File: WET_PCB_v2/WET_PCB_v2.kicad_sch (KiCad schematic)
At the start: 38 parts, among them J1 Barrel jack, J10 POGO1, J11 Conn_01x09_Pin, J12 Conn_01x09_Pin, J2 Power input, J3 Jumper, J35 Programming, J36 LED_POWER, J4 Coil plug, J5 Vsense_ADC1_IN1, J6 Pluggable Terminal Block, J7 Conn_01x09_Pin, J8 Conn_01x09_Pin, J9 POGO2, U1 Opamp_Quad

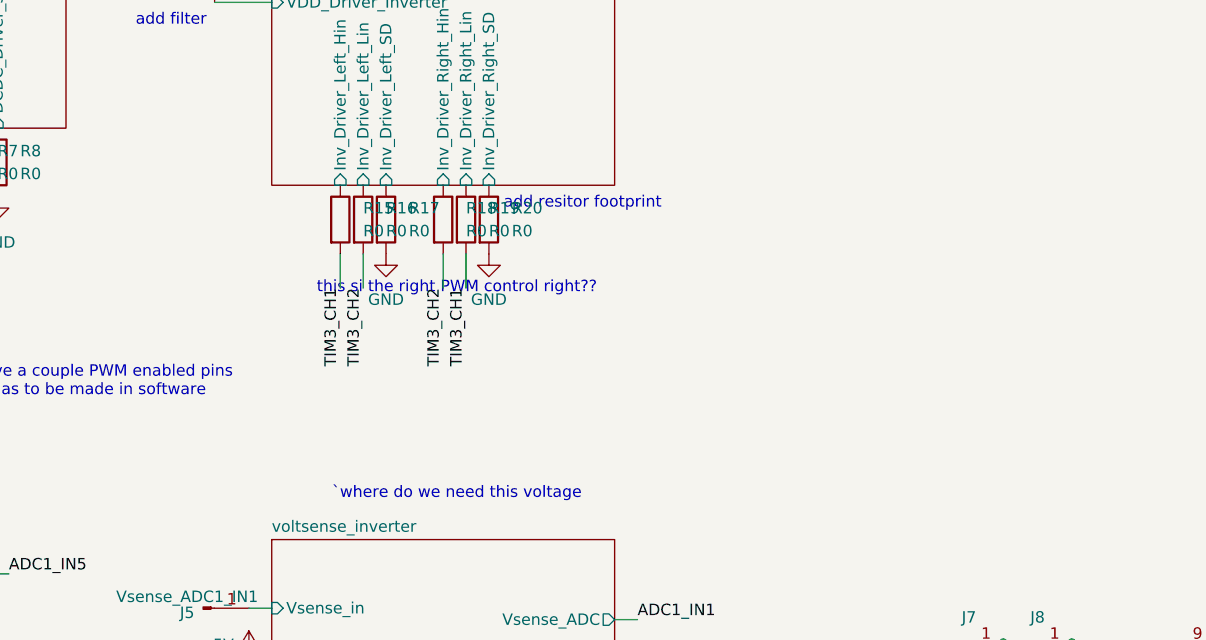
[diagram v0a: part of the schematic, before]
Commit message: most routing done. to do: 12v routing, test points, deco, checking clearance
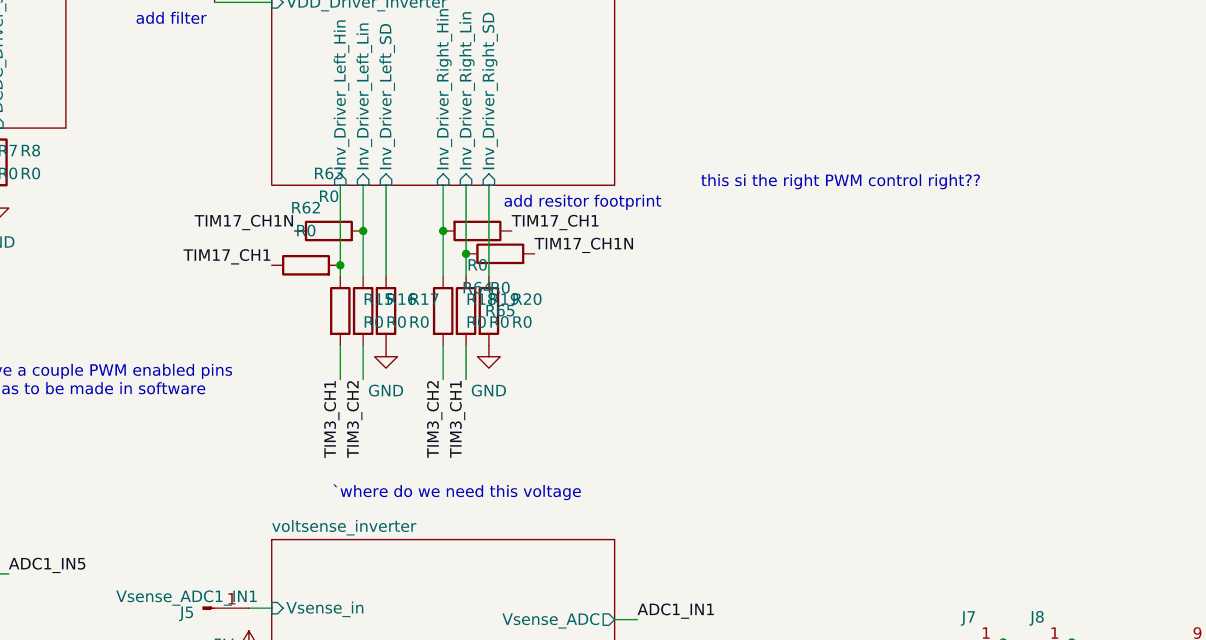
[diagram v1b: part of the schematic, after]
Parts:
- added R62, R63, R64, R65: R0, Resistor_SMD:R_0805_2012Metric_Pad1.20x1.40mm_HandSolder, symbol Device:R
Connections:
- net TIM17_CH1: now also R62.1, R64.1
- net TIM17_CH1N: now also R63.1, R65.2
- net inverter/Inv_Driver_Left_Hin: now also R62.2
- net inverter/Inv_Driver_Left_Lin: now also R63.2
- net inverter/Inv_Driver_Right_Hin: now also R64.2
- net inverter/Inv_Driver_Right_Lin: now also R65.1
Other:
- moved on the sheet: R15, R16, R17, R18, R19, R20

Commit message: fixed some mistakes added debug header
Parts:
- added J37: PRGM_DBG, Connector_PinSocket_2.54mm:PinSocket_1x02_P2.54mm_Vertical, symbol Connector:Conn_01x02_Pin
- J35: value Programming -> PRGM_DBG
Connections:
- net at J35.1 (Pin_1), J9.1 (Pin_1), U2.20 (POGO_PRG): now also J37.1 (Pin_1)
- net at J10.1 (Pin_1), J35.2 (Pin_2), U2.19 (POGO_PRG): now also J37.2 (Pin_2)
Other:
- note removed: "look for other UV LEDs"
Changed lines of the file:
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@@
 		)
 	)
-	(text "look for other UV LEDs"
-		(exclude_from_sim no)
-		(at 52.324 115.57 0)
-		(effects
-			(font
-				(size 1.27 1.27)
-			)
-		)
-	)
 	(text "`where do we need this voltage"
 		(exclude_from_sim no)
@@
 	)
 	(junction
+		(at 381 166.37)
+		(diameter 0)
+		(color 0 0 0 0)
+	)
+	(junction
 		(at 294.64 142.24)
 		(diameter 0)
@@
 	)
 	(junction
+		(at 378.46 170.18)
+		(diameter 0)
+		(color 0 0 0 0)
+	)
+	(junction
 		(at 370.84 162.56)
 		(diameter 0)
@@
 	(wire
 		(pts
+			(xy 378.46 170.18) (xy 384.81 170.18)
+		)
+		(stroke
+			(width 0)
+			(type default)
+		)
+	)
+	(wire
+		(pts
 			(xy 287.02 149.86) (xy 294.64 149.86)
 		)
@@
 	(wire
 		(pts
+			(xy 381 166.37) (xy 373.38 166.37)
+		)
+		(stroke
+			(width 0)
+			(type default)
+		)
+	)
+	(wire
+		(pts
 			(xy 132.08 146.05) (xy 134.62 146.05)
 		)
@@
 	(wire
 		(pts
+			(xy 378.46 170.18) (xy 378.46 172.72)
+		)
+		(stroke
+			(width 0)
+			(type default)
+		)
+	)
+	(wire
+		(pts
 			(xy 287.02 152.4) (xy 294.64 152.4)
 		)
@@
 	(wire
 		(pts
+			(xy 381 166.37) (xy 381 172.72)
+		)
+		(stroke
+			(width 0)
+			(type default)
+		)
+	)
+	(wire
+		(pts
 			(xy 29.21 38.1) (xy 39.37 38.1)
 		)
@@
 	(wire
 		(pts
-			(xy 382.27 166.37) (xy 373.38 166.37)
+			(xy 382.27 166.37) (xy 381 166.37)
 		)
 		(stroke
@@
 	(wire
 		(pts
-			(xy 367.03 170.18) (xy 384.81 170.18)
+			(xy 367.03 170.18) (xy 378.46 170.18)
 		)
 		(stroke
@@
 			)
 		)
-		(property "Value" "Programming"
-			(at 387.604 159.766 0)
+		(property "Value" "PRGM_DBG"
+			(at 391.922 164.846 90)
 			(show_name no)
 			(do_not_autoplace no)
@@
 					(unit 1)
 				)
+			)
+		)
+	)
+	(symbol
+		(lib_id "Connector:Conn_01x02_Pin")
+		(at 378.46 177.8 90)
+		(unit 1)
+		(body_style 1)
+		(exclude_from_sim no)
+		(in_bom yes)
+		(on_board yes)
+		(in_pos_files yes)
+		(dnp no)
+		(property "Reference" "J37"
+			(at 381.762 176.276 0)
+			(show_name no)
+			(do_not_autoplace no)
+			(effects
+				(font
+					(size 1.27 1.27)
+				)
+			)
+		)
+		(property "Value" "PRGM_DBG"
+			(at 379.222 180.086 90)
+			(show_name no)
+			(do_not_autoplace no)
+			(effects
+				(font
+					(size 1.27 1.27)
+				)
+			)
+		)
+		(property "Footprint" "Connector_PinSocket_2.54mm:PinSocket_1x02_P2.54mm_Vertical"
+			(at 378.46 177.8 0)
+			(hide yes)
+			(show_name no)
+			(do_not_autoplace no)
+			(effects
+				(font
+					(size 1.27 1.27)
+				)
+			)
+		)
+		(property "Datasheet" ""
+			(at 378.46 177.8 0)
+			(hide yes)
+			(show_name no)
+			(do_not_autoplace no)
+			(effects
+				(font
+					(size 1.27 1.27)
+				)
+			)
+		)
+		(property "Description" "Generic connector, single row, 01x02, script generated"
+			(at 378.46 177.8 0)
+			(hide yes)
+			(show_name no)
+			(do_not_autoplace no)
+			(effects
+				(font
+					(size 1.27 1.27)
+				)
+			)
+		)
+		(pin "1"
+		)
+		(pin "2"
+		)
+		(instances
+			(project "WET_PCB_v2"
+				(path "/13451c35-1666-47d9-9525-8d8125ba1cf3"
+					(reference "J37")
+					(unit 1)
+				)

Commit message: labels
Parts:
- renumbered R3 to JMP1, R15 to JMP10, R16 to JMP11, R17 to JMP12, R18 to JMP13, R19 to JMP14, R64 to JMP15, R20 to JMP16, R65 to JMP17, R5 to JMP2, R6 to JMP3, R7 to JMP4, R8 to JMP5, R12 to JMP6, R14 to JMP7, R62 to JMP8, R63 to JMP9
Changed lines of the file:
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@@
 		(dnp no)
 		(fields_autoplaced yes)
-		(property "Reference" "R15"
+		(property "Reference" "JMP10"
 			(at 215.9 99.0599 0)
 			(show_name no)
@@
 			(project "WET_PCB_v2"
 				(path "/13451c35-1666-47d9-9525-8d8125ba1cf3"
-					(reference "R15")
+					(reference "JMP10")
 					(unit 1)
 				)
@@
 		(dnp no)
 		(fields_autoplaced yes)
-		(property "Reference" "R20"
+		(property "Reference" "JMP16"
 			(at 232.41 99.0599 0)
 			(show_name no)
@@
 			(project "WET_PCB_v2"
 				(path "/13451c35-1666-47d9-9525-8d8125ba1cf3"
-					(reference "R20")
+					(reference "JMP16")
 					(unit 1)
 				)
@@
 		(dnp no)
 		(fields_autoplaced yes)
-		(property "Reference" "R19"
+		(property "Reference" "JMP14"
 			(at 229.87 99.0599 0)
 			(show_name no)
@@
 			(project "WET_PCB_v2"
 				(path "/13451c35-1666-47d9-9525-8d8125ba1cf3"
-					(reference "R19")
+					(reference "JMP14")
 					(unit 1)
 				)
@@
 		(dnp no)
 		(fields_autoplaced yes)
-		(property "Reference" "R18"
+		(property "Reference" "JMP13"
 			(at 227.33 99.0599 0)
 			(show_name no)
@@
 			(project "WET_PCB_v2"
 				(path "/13451c35-1666-47d9-9525-8d8125ba1cf3"
-					(reference "R18")
+					(reference "JMP13")
 					(unit 1)
 				)
@@
 		(dnp no)
 		(fields_autoplaced yes)
-		(property "Reference" "R3"
+		(property "Reference" "JMP1"
 			(at 152.4 87.6299 0)
 			(show_name no)
@@
 			(project "WET_PCB_v2"
 				(path "/13451c35-1666-47d9-9525-8d8125ba1cf3"
-					(reference "R3")
+					(reference "JMP1")
 					(unit 1)
 				)
@@
 		(dnp no)
 		(fields_autoplaced yes)
-		(property "Reference" "R64"
+		(property "Reference" "JMP15"
 			(at 228.6 97.79 90)
 			(show_name no)
@@
 			(project "WET_PCB_v2"
 				(path "/13451c35-1666-47d9-9525-8d8125ba1cf3"
-					(reference "R64")
+					(reference "JMP15")
 					(unit 1)
 				)
@@
 		(dnp no)
 		(fields_autoplaced yes)
-		(property "Reference" "R62"
+		(property "Reference" "JMP8"
 			(at 209.55 88.9 90)
 			(show_name no)
@@
 			(project "WET_PCB_v2"
 				(path "/13451c35-1666-47d9-9525-8d8125ba1cf3"
-					(reference "R62")
+					(reference "JMP8")
 					(unit 1)
 				)
@@
 		(dnp no)
 		(fields_autoplaced yes)
-		(property "Reference" "R17"
+		(property "Reference" "JMP12"
 			(at 220.98 99.0599 0)
 			(show_name no)
@@
 			(project "WET_PCB_v2"
 				(path "/13451c35-1666-47d9-9525-8d8125ba1cf3"
-					(reference "R17")
+					(reference "JMP12")
 					(unit 1)
 				)
@@
 		(dnp no)
 		(fields_autoplaced yes)
-		(property "Reference" "R5"
+		(property "Reference" "JMP2"
 			(at 160.02 87.6299 0)
 			(show_name no)
@@
 			(project "WET_PCB_v2"
 				(path "/13451c35-1666-47d9-9525-8d8125ba1cf3"
-					(reference "R5")
+					(reference "JMP2")
 					(unit 1)
 				)
@@
 	)
 	(symbol
+		(lib_name "R_1")
 		(lib_id "Device:R")
 		(at 175.26 83.82 0)
@@
 		(dnp no)
 		(fields_autoplaced yes)
-		(property "Reference" "R8"
+		(property "Reference" "JMP5"
 			(at 177.8 82.5499 0)
 			(show_name no)
@@
 			(project "WET_PCB_v2"
 				(path "/13451c35-1666-47d9-9525-8d8125ba1cf3"
-					(reference "R8")
+					(reference "JMP5")
 					(unit 1)
 				)
@@
 		(dnp no)
 		(fields_autoplaced yes)
-		(property "Reference" "R16"
+		(property "Reference" "JMP11"
 			(at 218.44 99.0599 0)
 			(show_name no)
@@
 			(project "WET_PCB_v2"
 				(path "/13451c35-1666-47d9-9525-8d8125ba1cf3"
-					(reference "R16")
+					(reference "JMP11")
 					(unit 1)
 				)
@@
 		(dnp no)
 		(fields_autoplaced yes)
-		(property "Reference" "R65"
+		(property "Reference" "JMP17"
 			(at 231.14 100.33 90)
 			(show_name no)
@@
 			(project "WET_PCB_v2"
 				(path "/13451c35-1666-47d9-9525-8d8125ba1cf3"
-					(reference "R65")
+					(reference "JMP17")
 					(unit 1)
 				)
@@
 		(dnp no)
 		(fields_autoplaced yes)
-		(property "Reference" "R7"
+		(property "Reference" "JMP4"
 			(at 175.26 82.5499 0)
 			(show_name no)
@@
 			(project "WET_PCB_v2"
 				(path "/13451c35-1666-47d9-9525-8d8125ba1cf3"
-					(reference "R7")
+					(reference "JMP4")
 					(unit 1)
 				)
@@
 		(dnp no)
 		(fields_autoplaced yes)
-		(property "Reference" "R12"
+		(property "Reference" "JMP6"
 			(at 184.15 53.3876 0)
 			(show_name no)
@@
 			(project "WET_PCB_v2"
 				(path "/13451c35-1666-47d9-9525-8d8125ba1cf3"
-					(reference "R12")
+					(reference "JMP6")
 					(unit 1)
 				)
@@
 		(dnp no)
 		(fields_autoplaced yes)
-		(property "Reference" "R14"
+		(property "Reference" "JMP7"
 			(at 191.77 53.3401 0)
 			(show_name no)
@@
 			(project "WET_PCB_v2"
 				(path "/13451c35-1666-47d9-9525-8d8125ba1cf3"
-					(reference "R14")
+					(reference "JMP7")
 					(unit 1)
 				)
@@
 		(dnp no)
 		(fields_autoplaced yes)
-		(property "Reference" "R6"
+		(property "Reference" "JMP3"
 			(at 172.72 82.5499 0)
 			(show_name no)
@@
 			(project "WET_PCB_v2"
 				(path "/13451c35-1666-47d9-9525-8d8125ba1cf3"
-					(reference "R6")
+					(reference "JMP3")
 					(unit 1)
 				)
@@
 		(dnp no)
 		(fields_autoplaced yes)
-		(property "Reference" "R63"
+		(property "Reference" "JMP9"
 			(at 212.09 85.09 90)
 			(show_name no)
@@
 			(project "WET_PCB_v2"
 				(path "/13451c35-1666-47d9-9525-8d8125ba1cf3"
-					(reference "R63")
+					(reference "JMP9")
 					(unit 1)
 				)

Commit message: finished and added some drawings
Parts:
- added J38, J41, J42: TEST, Connector_PinSocket_2.54mm:PinSocket_1x01_P2.54mm_Vertical, symbol Connector:Conn_01x01_Pin
- added J43, J44, J45: PRGM_DBG, Connector_PinSocket_2.54mm:PinSocket_1x02_P2.54mm_Vertical, symbol Connector:Conn_01x02_Pin
- D1, D2: footprint LED_THT:LED_D3.0mm -> LED_SMD:LED_PLCC-2_3.4x3.0mm_AK
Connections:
- net DCDC/DCDC_coil_circuit_side: now also J42.1 (Pin_1)
- net DCDC/DCDC_coil_input_side: now also J41.1 (Pin_1)
- net DCDC/VoutDCDC: now also J43.1 (Pin_1)
- net DCDC/currsense_FET_side: now also J44.2 (Pin_2)
- net DCDC/currsense_cap_side: now also J44.1 (Pin_1)
- net VPP: now also J38.1 (Pin_1)
- net inverter/Vin_Inverter: now also J43.2 (Pin_2)
- net inverter/Vout_Inverter_+: now also J45.2 (Pin_2)
- net inverter/Vout_Inverter_-: now also J45.1 (Pin_1)

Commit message: cleaned up schematics, added power LED
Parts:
- removed J38, J42: TEST, Connector_PinSocket_2.54mm:PinSocket_1x01_P2.54mm_Vertical, symbol Connector:Conn_01x01_Pin
- removed J44: PRGM_DBG, Connector_PinSocket_2.54mm:PinSocket_1x02_P2.54mm_Vertical, symbol Connector:Conn_01x02_Pin
- added D3: LED, LED_SMD:LED_PLCC-2_3.4x3.0mm_AK, symbol Device:LED
- added H1, H2, H3: MountingScrew, MountingHole:MountingHole_3.2mm_M3_ISO14580, symbol Auxiliary_Items:MountingScrew
- added J39, J40: TEST, Connector_PinSocket_2.54mm:PinSocket_1x01_P2.54mm_Vertical, symbol Connector:Conn_01x01_Pin
- added J44, J46, J47: GND, Connector_PinSocket_2.54mm:PinSocket_1x01_P2.54mm_Vertical, symbol Connector:Conn_01x01_Pin
- added R3: R, Resistor_SMD:R_0805_2012Metric_Pad1.20x1.40mm_HandSolder, symbol Device:R
- J3: value Jumper -> 5v source select
- J43, J45: value PRGM_DBG -> TEST
- J6: value Pluggable Terminal Block -> TX Coil out
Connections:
- net DCDC/currsense_FET_side: now also J40.1 (Pin_1)
- net DCDC/currsense_cap_side: now also J39.1 (Pin_1)
- net GND: now also D3.1 (K), J44.1 (Pin_1), J46.1 (Pin_1), J47.1 (Pin_1)
- net VPP: now also R3.1
- new net: D3.2 (A), R3.2
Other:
- note added: "Aqua Verde DCDC - inverter board"
- note added: "Converters and current sensing"
- note added: "Decoration"
- note added: "External current measurement"
- note added: "MCU connections"
- note added: "Mounting hardware"
- note added: "Option for TIM17 or TIM3"
- note added: "Power in"
- note added: "Test ground connectors"
- note added: "Voltage measurement"
- note removed: "12V lower if all ICs can go lower to recuse the LDO's work"
- note removed: "`where do we need this voltage"
- note removed: "add 0ohm"
- note removed: "add filter"
- note removed: "add footprint to add wires trough current measurement"
- note removed: "add resitor footprint"
- note removed: "do we want an input protection diode? we can also place it and short it in the final PCB"
- note removed: "i did not add any testpoints we should check out where we need them"
- note removed: "it feels kinda odd to not have ugeass caps, i think were missing something"
- note removed: "theres no PWM ch left so might be fun to so it adjusting its dutycycle for the DCDC"
- note removed: "this si the right PWM control right??"
- note removed: "we only have a couple PWM enabled pins so this has to be made in software"
- moved on the sheet: C1, C2, C3, D1, D2, J1, J10, J11, J12, J3, J35, J36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

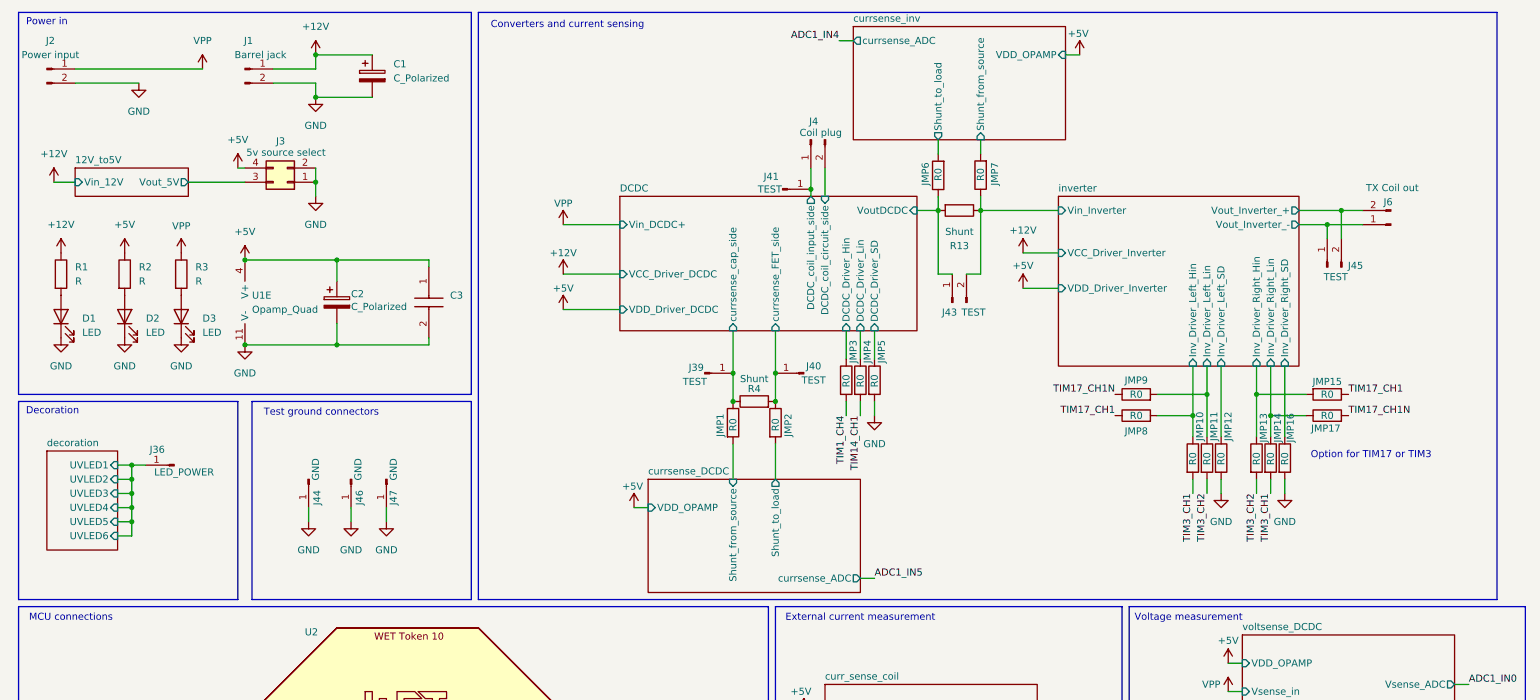
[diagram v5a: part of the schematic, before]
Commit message: some caps were missing and wrong way around AAAAAAAAAAAAAAAAAAAAAAAAAAAAAAAAAAA
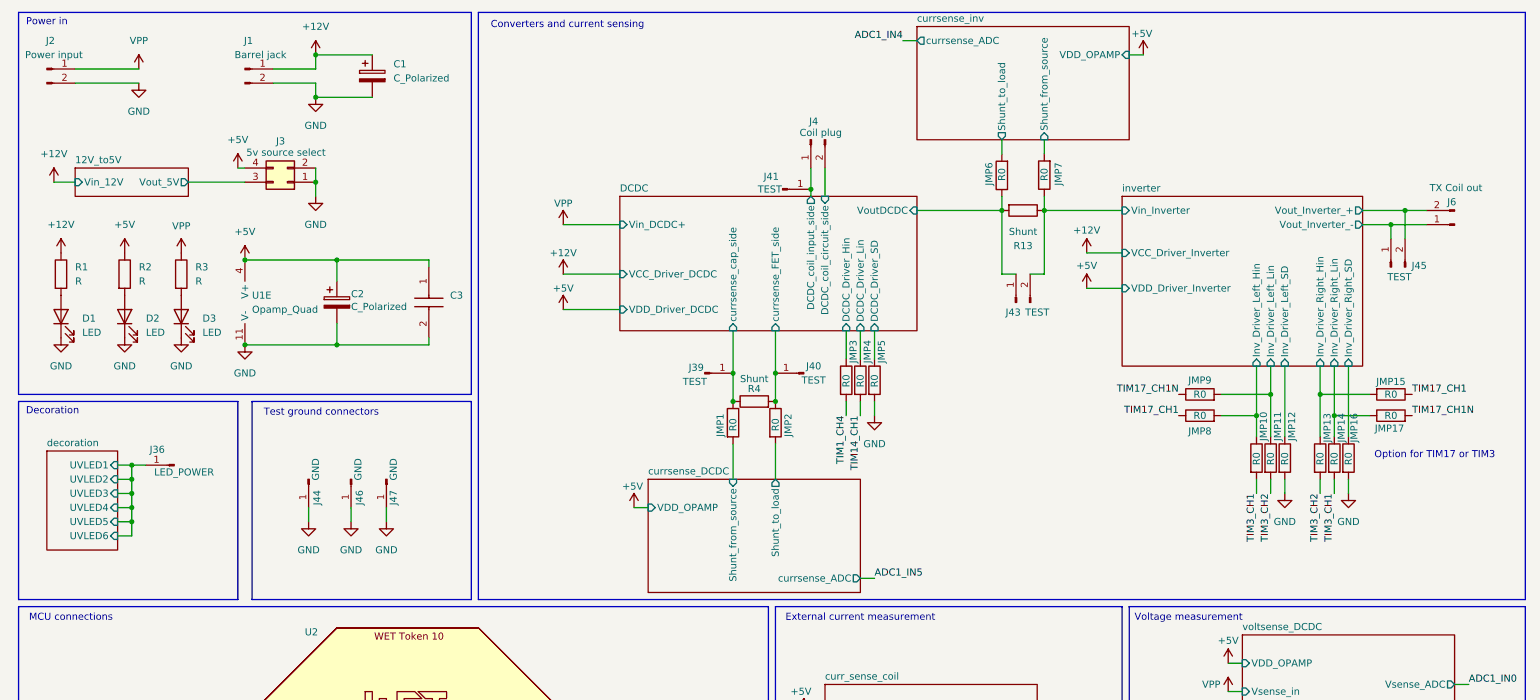
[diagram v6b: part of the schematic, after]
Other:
- moved on the sheet: J43, J45, J6, JMP10, JMP11, JMP12, JMP13, JMP14, JMP15, JMP16, JMP17, JMP6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

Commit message: imma hand it in now
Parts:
- removed J45: TEST, Connector_PinSocket_2.54mm:PinSocket_1x02_P2.54mm_Vertical, symbol Connector:Conn_01x02_Pin
- added H4: MountingScrew, MountingHole:MountingHole_3.2mm_M3_ISO14580, symbol Auxiliary_Items:MountingScrew
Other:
- moved on the sheet: J5
